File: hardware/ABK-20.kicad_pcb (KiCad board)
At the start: 2 copper layers, 175 x 80 mm, 69 parts, among them J1 CONN_01X04, J2 CONN_01X04, J4 Con_3-5V, J5 USB_C_6P, J6 Sync_Jumper, SW1 SW_SPST, SW2 SW_Push_LED, SW3 SW_SPDT_MSM, SW4 SW_Push, U1 ATTINY85-20SU, U2 PAM8002, U3 7805

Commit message: Sync schematic and PCB: restore BT1/BT2/J3 and fix Jack1/Jack2 pin 6
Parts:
- C1, C2, C3, C4, C5, C6, C7, C8, D1, D2, D3, R1, R10, R11, R12, R13, R14, R15, R16, R17, R18, R2, R3, R4, R5, R6, R7, R8, R9, R99: moved to B.Cu
- moved D1 164.9 mm to (69.1, 164.7)
- moved D2 151.9 mm to (69.1, 154.7)
- moved D3 140.5 mm to (69.1, 144.7)
- moved R99 66.7 mm to (140.5, 122.7)
- moved C1 64.5 mm to (96.9, 188.3)
- moved R10 59.3 mm to (140.5, 185.7)
- moved R1 58.5 mm to (127.6, 185.3)
- moved R9 53.5 mm to (127.6, 129.3)
- moved R18 52.7 mm to (140.5, 129.7)
- moved C8 48.9 mm to (96.9, 131.6)
- moved C2 47.1 mm to (96.9, 179.6)
- moved R11 45.3 mm to (140.5, 178.7)
- moved R2 44.5 mm to (127.6, 178.3)
- moved R8 39.5 mm to (127.6, 136.3)
- moved R17 38.7 mm to (140.5, 136.7)
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
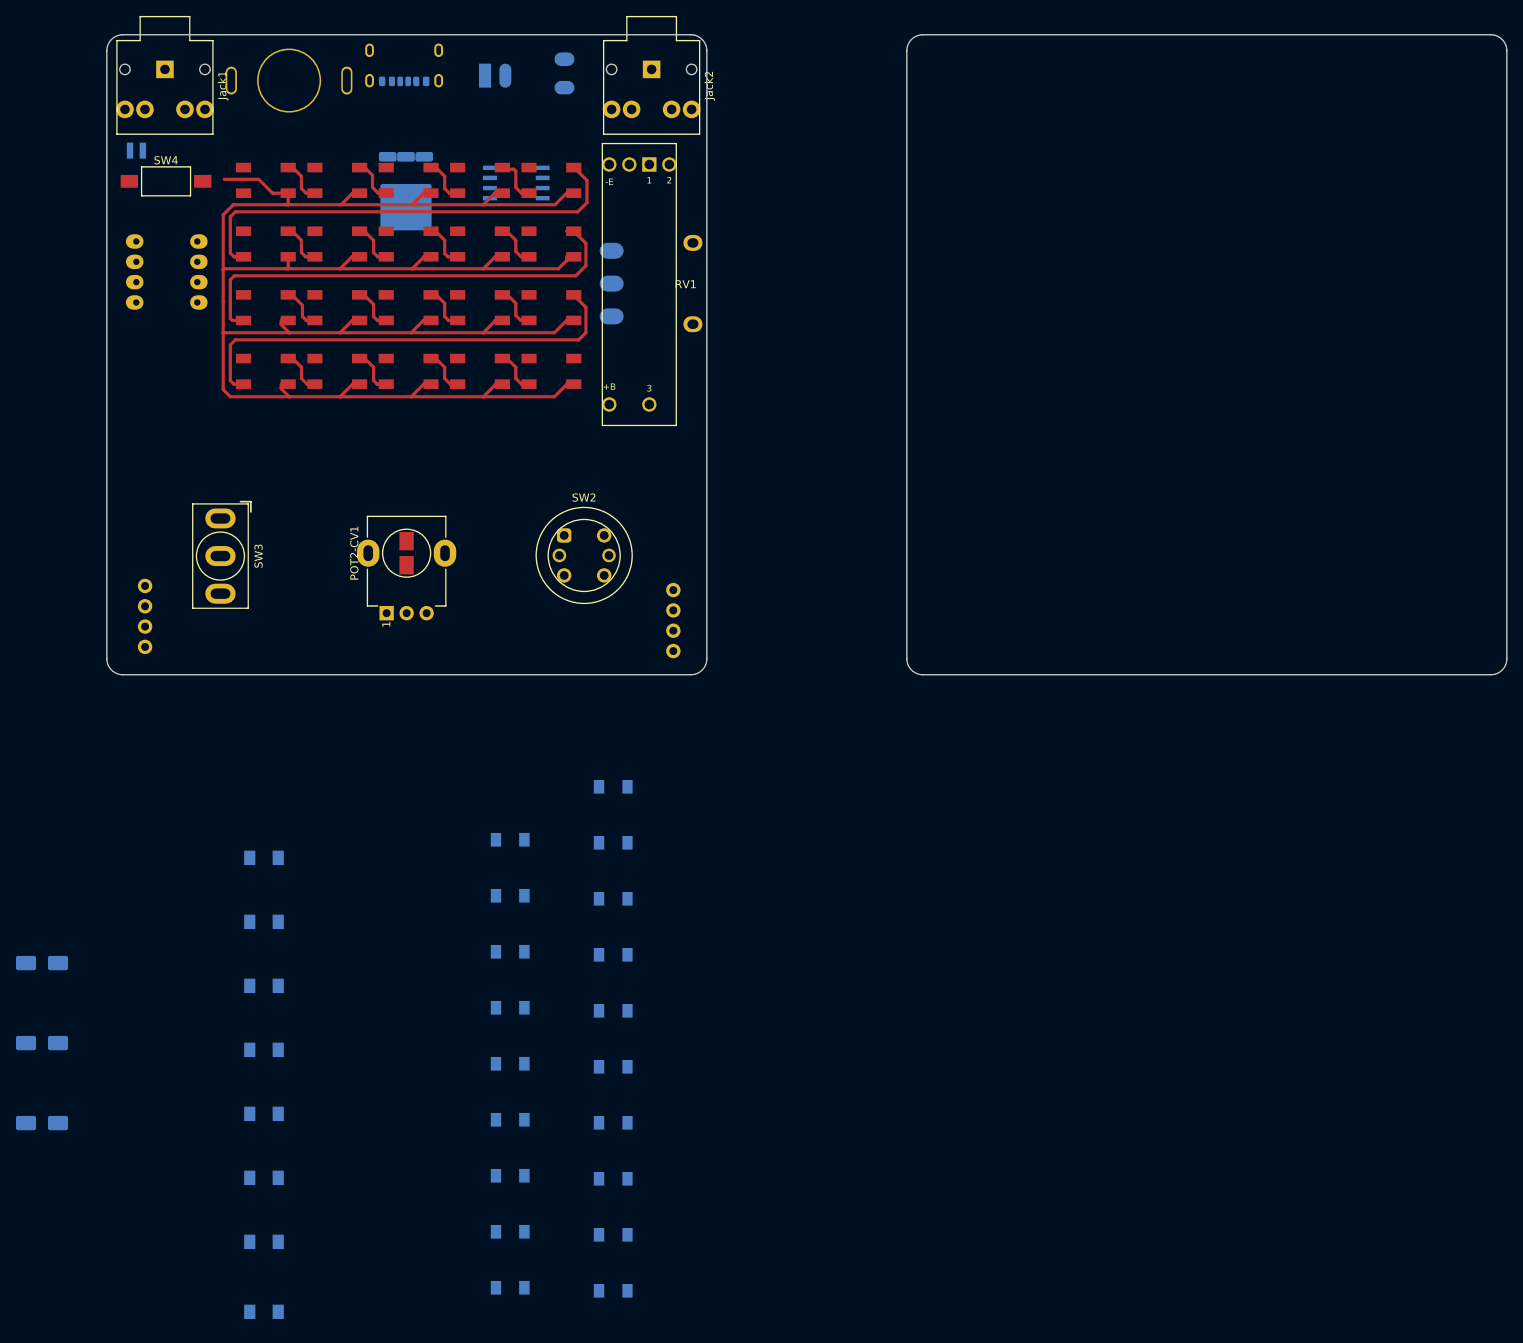
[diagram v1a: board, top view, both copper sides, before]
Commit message: feat(hardware): complete 75x80 mm PCB routing, interactive BOM, 3D models and gerbers
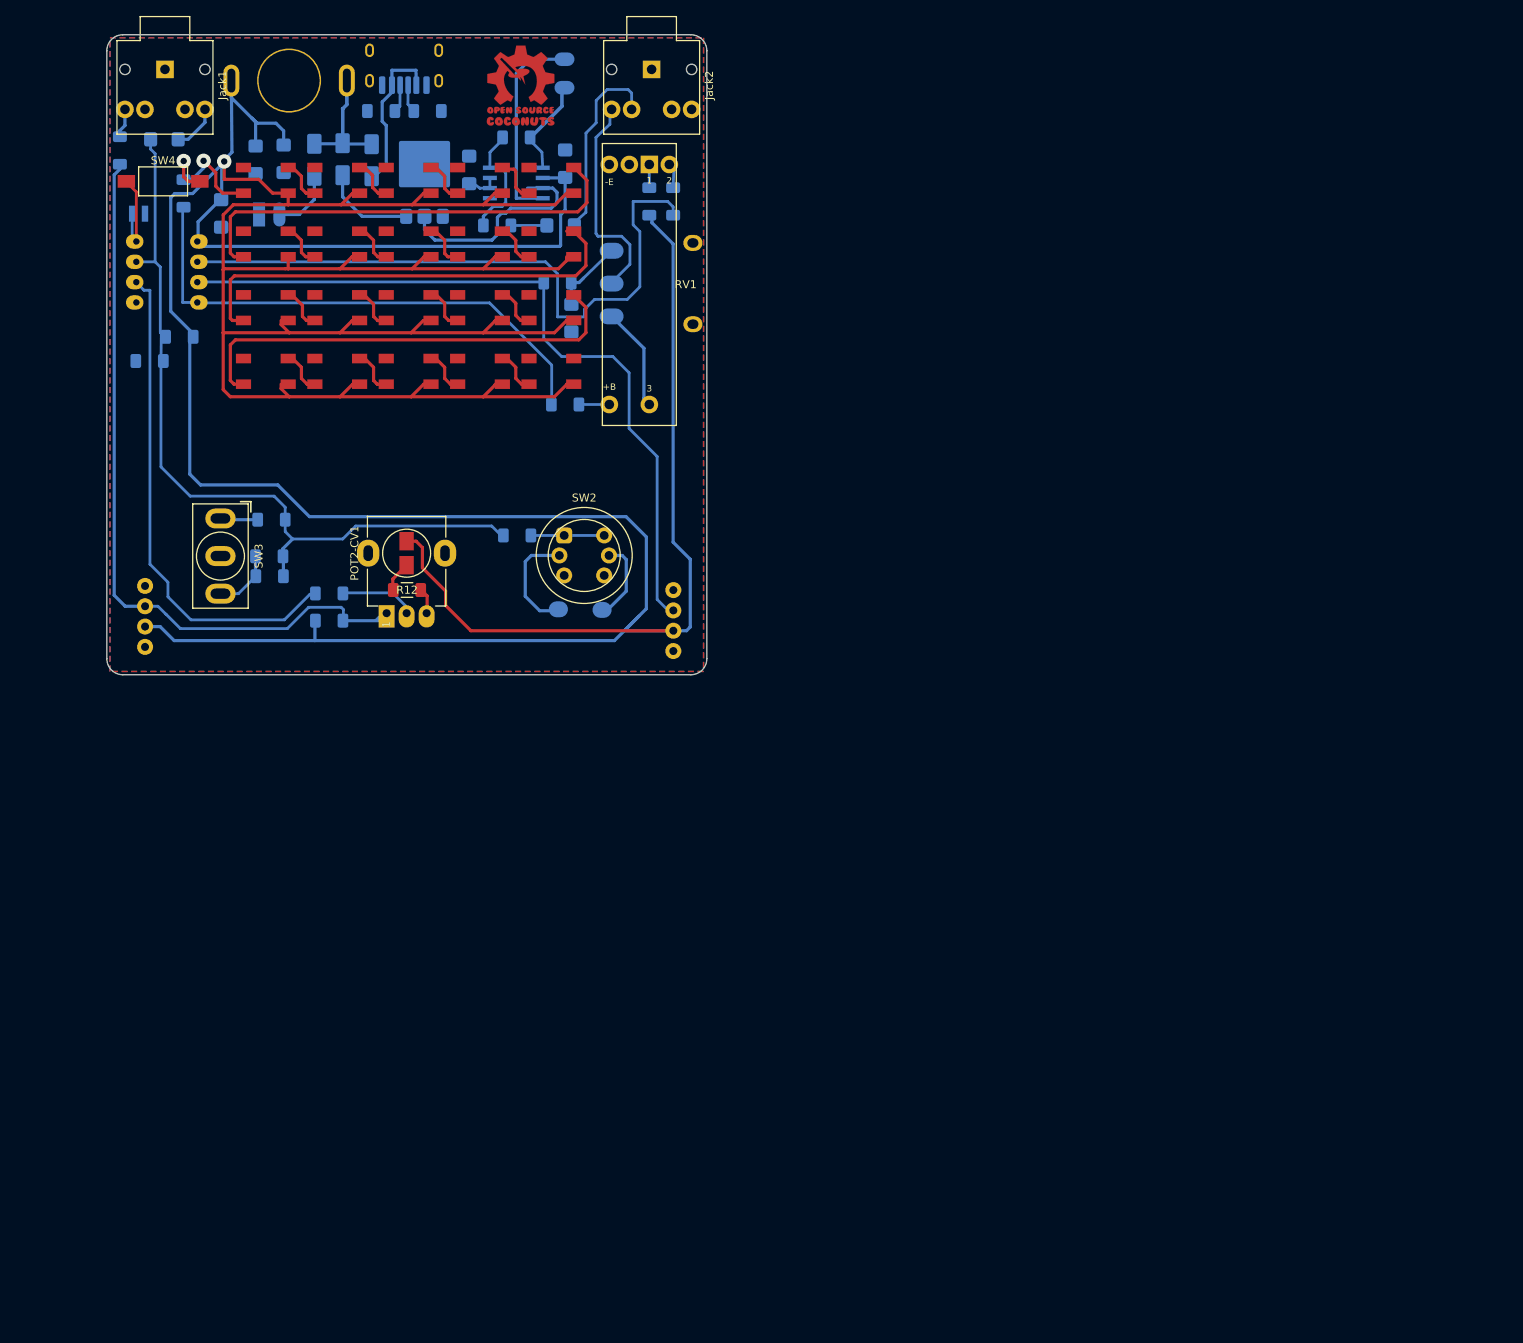
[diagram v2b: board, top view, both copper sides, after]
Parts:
- added ?: , , F.Cu at (139.1, 100.6)
- added Pad4: SP - b, 007_dusjagr:PiezoPad_smd, B.Cu at (133.7, 100.5)
- added Ref**: Val**, 007_dusjagr:Coconut_logo_sm, F.Cu at (128.8, 35.0)
- C1, C2, C3, C4, C5, C6, C7, C8: footprint 8Bitmixtape_reworked:C_1206_HandSoldering -> 007_dusjagr:C_1210_noGND
- R1, R10, R11, R13, R14, R15, R16, R17, R18, R2, R3, R4, R5, R6, R7, R8, R9, R99: footprint 8Bitmixtape_reworked:R_1206_HandSoldering -> 007_dusjagr:R_1206_noGND_sm
- R12: footprint 8Bitmixtape_reworked:R_1206_HandSoldering -> 007_dusjagr:R_1206_noGND_sm; moved to F.Cu
- U3: footprint Package_TO_SOT_SMD:TO-252-3_TabPin2 -> 8Bitmixtape_reworked:TO-252-3_TabPin2
- moved C1 147.1 mm to (84.4, 41.7), turned to 180 degrees
- moved C2 135.3 mm to (95.8, 44.3), turned to -90 degrees
- moved R11 129.3 mm to (145.0, 49.5), turned to 90 degrees
- moved D1 126.2 mm to (106.7, 44.2), turned to -90 degrees
- moved R1 125.9 mm to (86.3, 66.4), turned to 180 degrees
- moved C4 119.4 mm to (99.3, 44.2), turned to -90 degrees
- moved R2 117.8 mm to (82.5, 69.4), turned to 180 degrees
- moved D2 117.8 mm to (110.3, 44.3), turned to -90 degrees
- moved C3 114.1 mm to (135.3, 64.1), turned to -90 degrees
- moved R15 109.8 mm to (128.4, 41.5), turned to 180 degrees
- moved C5 109.5 mm to (133.9, 52.5)
- moved R14 106.2 mm to (126.0, 52.5)
- moved D3 106.0 mm to (103.1, 44.3), turned to -90 degrees
- moved C6 105.2 mm to (122.5, 45.6), turned to 90 degrees
- moved R17 102.7 mm to (111.5, 38.2), turned to 180 degrees
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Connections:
- J2 pad 4: Sync_OUT -> unconnected-(J2-P4-Pad4)
- Jack2 pad 3: Sync_OUT -> unconnected-(Jack2-R-Pad3)
- Jack2 pad 4: unconnected-(Jack2-SN-Pad4) -> Sound_OUT
- Jack2 pad 5: Sound_OUT -> unconnected-(Jack2-RN-Pad5)
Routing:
- net VCC: track 237.8 -> 621.5 mm, vias 0 -> 1
- net PB3: track 0.00 -> 98.4 mm
- net CV_IN: track 0.00 -> 96.0 mm
- net PB1: track 0.00 -> 95.3 mm
- net PB2/A1: track 0.00 -> 80.8 mm
- net PB0: track 0.00 -> 66.2 mm
- net PB4/A2: track 0.00 -> 62.3 mm
- net GND: track 0.00 -> 48.7 mm, vias 0 -> 1
- net Net-(Jack2-T): track 0.00 -> 27.0 mm
- net Net-(U2-OUT+): track 0.00 -> 25.7 mm
- net Sound_OUT: track 0.00 -> 24.2 mm
- net Net-(D2-A): track 0.00 -> 19.3 mm
- net Net-(D1-K): track 0.00 -> 16.4 mm
- net Net-(U2--IN): track 0.00 -> 15.0 mm
- net unconnected-(SW2-PadA): track 0.00 -> 13.6 mm
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- added copper zone on B.Cu, net GND
- added copper zone on F.Cu, net GND
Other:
- board size 175 x 80 mm -> 75 x 80 mm

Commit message: deleted files
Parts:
- added BT2: Battery_Cell, 8Bitmixtape_reworked:BAT_Holder_AAA-new_noHole, F.Cu at (200.5, 66.4)
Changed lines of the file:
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@@
+		)
+	)
+	(footprint "8Bitmixtape_reworked:BAT_Holder_AAA-new_noHole"
+		(layer "F.Cu")
+		(at 200.533 66.421)
+		(property "Reference" "BT2"
+			(at 0 -3.81 0)
+			(layer "Eco2.User")
+			(effects
+				(font
+					(size 1 1)
+					(thickness 0.15)
+				)
+			)
+		)
+		(property "Value" "Battery_Cell"
+			(at 0.254 3.81 0)
+			(layer "Eco2.User")
+			(effects
+				(font
+					(size 1 1)
+					(thickness 0.15)
+				)
+			)
+		)
+		(property "Datasheet" ""
+			(at 0 0 0)
+			(layer "F.Fab")
+			(hide yes)
+			(effects
+				(font
+					(size 1.27 1.27)
+					(thickness 0.15)
+				)
+			)
+		)
+		(property "Description" ""
+			(at 0 0 0)
+			(layer "F.Fab")
+			(hide yes)
+			(effects
+				(font
+					(size 1.27 1.27)
+					(thickness 0.15)
+				)
+			)
+		)
+		(attr through_hole)
+		(fp_line
+			(start 23.662 0.134)
+			(end 23.662 -0.366)
+			(stroke
+				(width 0.1524)
+				(type solid)
+			)
+			(layer "F.SilkS")
+		)
+		(fp_line
+			(start 23.662 0.134)
+			(end 24.162 0.134)
+			(stroke
+				(width 0.1524)
+				(type solid)
+			)
+			(layer "F.SilkS")
+		)
+		(fp_line
+			(start 24.162 -0.766)
+			(end 24.562 -0.766)
+			(stroke
+				(width 0.1524)
+				(type solid)
+			)
+			(layer "F.SilkS")
+		)
+		(fp_line
+			(start 24.162 -0.366)
+			(end 23.662 -0.366)
+			(stroke
+				(width 0.1524)
+				(type solid)
+			)
+			(layer "F.SilkS")
+		)
+		(fp_line
+			(start 24.162 -0.366)
+			(end 24.162 -0.766)
+			(stroke
+				(width 0.1524)
+				(type solid)
+			)
+			(layer "F.SilkS")
+		)
+		(fp_line
+			(start 24.162 0.534)
+			(end 24.162 0.134)
+			(stroke
+				(width 0.1524)
+				(type solid)
+			)
+			(layer "F.SilkS")
+		)
+		(fp_line
+			(start 24.562 -0.766)
+			(end 24.562 -0.366)
+			(stroke
+				(width 0.1524)
+				(type solid)
+			)
+			(layer "F.SilkS")
+		)
+		(fp_line
+			(start 24.562 -0.366)
+			(end 25.062 -0.366)
+			(stroke
+				(width 0.1524)
+				(type solid)
+			)
+			(layer "F.SilkS")
+		)
+		(fp_line
+			(start 24.562 0.134)
+			(end 24.562 0.534)
+			(stroke
+				(width 0.1524)
+				(type solid)
+			)
+			(layer "F.SilkS")
+		)
+		(fp_line
+			(start 24.562 0.534)
+			(end 24.162 0.534)
+			(stroke
+				(width 0.1524)
+				(type solid)
+			)
+			(layer "F.SilkS")
+		)
+		(fp_line
+			(start 25.062 -0.366)
+			(end 25.062 0.134)
+			(stroke
+				(width 0.1524)
+				(type solid)
+			)
+			(layer "F.SilkS")
+		)
+		(fp_line
+			(start 25.062 0.134)
+			(end 24.562 0.134)
+			(stroke
+				(width 0.1524)
+				(type solid)
+			)
+			(layer "F.SilkS")
+		)
+		(fp_line
+			(start -27.18 -5.786)
+			(end -27.178 5.334)
+			(stroke
+				(width 0.15)
+				(type solid)
+			)
+			(layer "Eco2.User")
+		)
+		(fp_line
+			(start -27.18 -5.786)
+			(end 27.18 -5.786)
+			(stroke
+				(width 0.15)
+				(type solid)
+			)
+			(layer "Eco2.User")
+		)
+		(fp_line
+			(start -27.18 5.334)
+			(end 27.18 5.334)
+			(stroke
+				(width 0.15)
+				(type solid)
+			)
+			(layer "Eco2.User")
+		)
+		(fp_line
+			(start 27.178 5.334)
+			(end 27.18 -5.786)
+			(stroke
+				(width 0.15)
+				(type solid)
+			)
+			(layer "Eco2.User")
+		)
+		(fp_line
+			(start 31 -0.116)
+			(end -31 -0.116)
+			(stroke
+				(width 0.1524)
+				(type solid)
+			)
+			(layer "Eco2.User")
+		)
+		(pad "1" smd rect
+			(at 29.5 -0.116)
+			(size 4 7)
+			(layers "F.Cu" "F.Mask" "F.Paste")
+			(solder_mask_margin 0.01)
+		)
+		(pad "2" smd rect
+			(at -29.5 -0.116)
+			(size 4 7)
+			(layers "F.Cu" "F.Mask" "F.Paste")
+			(solder_mask_margin 0.01)
+		)
+		(embedded_fonts no)
+		(model "${KIPRJMOD}/3d_models/BatteryHolder_Keystone_2466_1xAAA.wrl"
+			(offset
+				(xyz 0 0 0)
+			)
+			(scale
+				(xyz 1 1 1)
+			)
+			(rotate
+				(xyz 0 0 0)
+			)
 		)
 	)
